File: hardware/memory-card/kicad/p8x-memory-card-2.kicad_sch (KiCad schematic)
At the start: 2 parts, among them U10 62256, U11 74HCT32

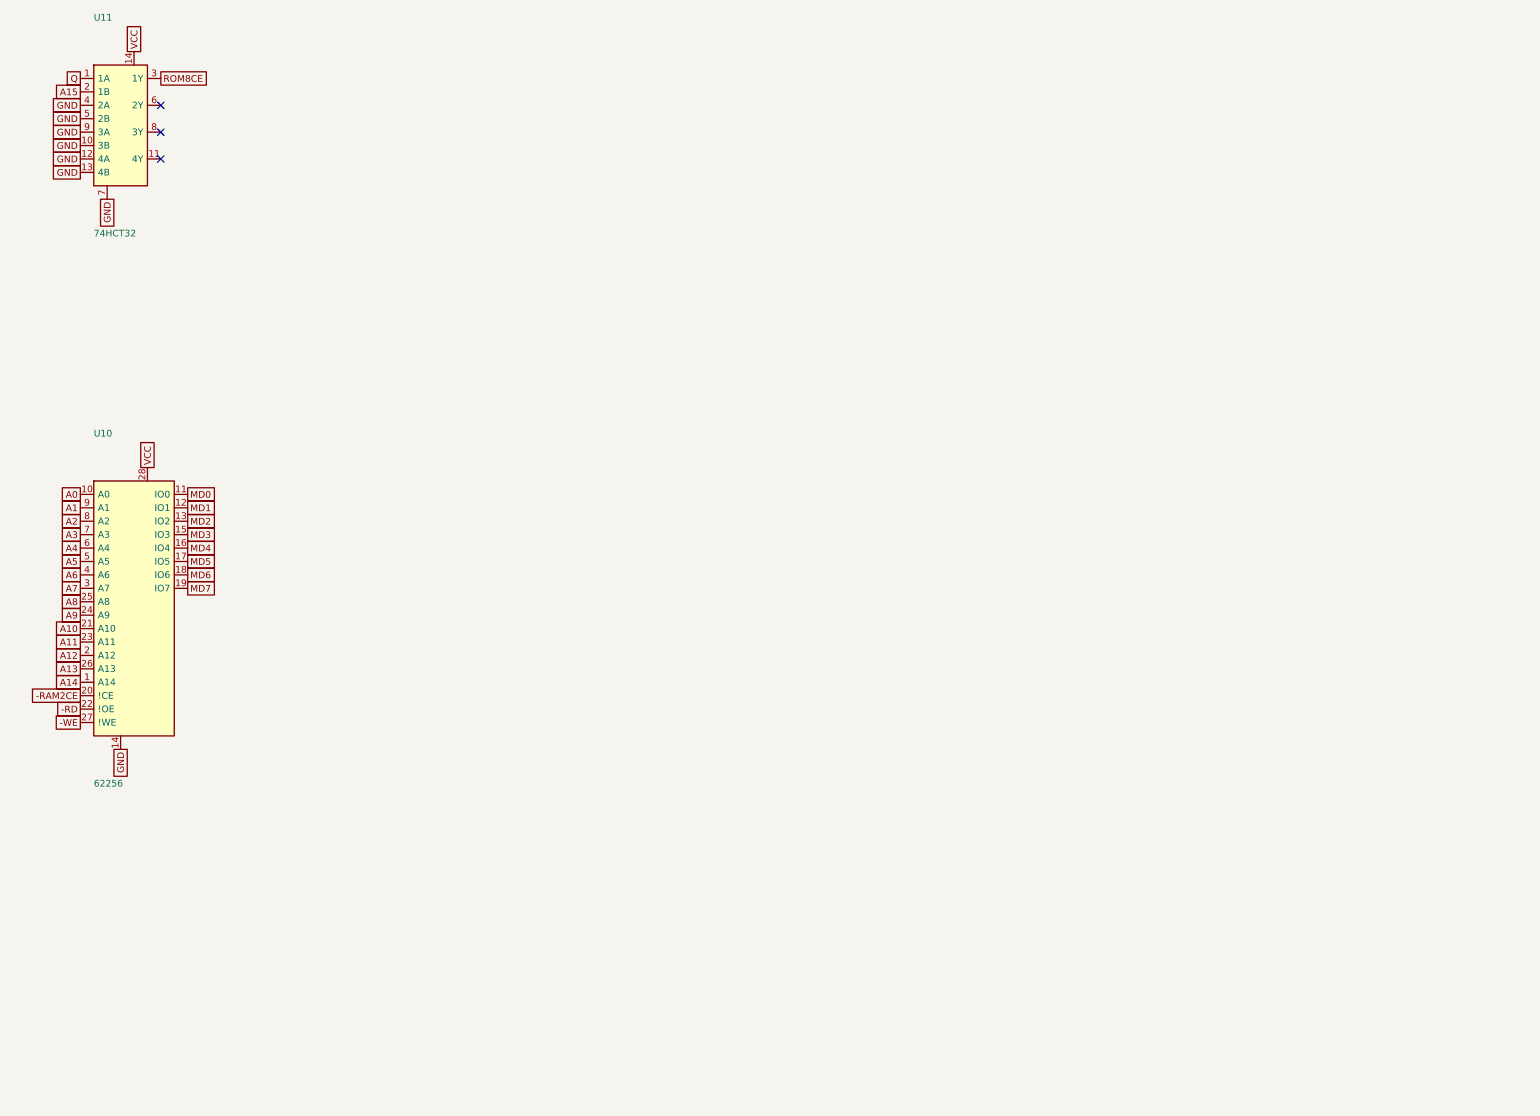
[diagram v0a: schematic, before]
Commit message: feat(sch): draw every P8X card schematic by function
Extend the functional-sheet grouping from the io-card to the control,
regbank, alu, memory, cf, ps2 and bustest cards. functional_sheets now
attaches unnamed glue gates, LEDs, resistors and connectors to the block
they share the most local nets with, so each block lists only its main
parts. A net with two or more pins on a sheet is now wired there even if
it continues elsewhere (its global name label rides on the wire), and
every wire is oriented by drawing side. The regbank gets one pointer per
sheet; the ps2 latches share a sheet with the AVR so the mailbox bus is
drawn. The bustest probe resistors use a straight-order RNISO8DSTR
drawing (the reversed B side forced every wire to cross and the sheet
fell back to labels). build_sch.sh now shows ELK fallbacks and clears old
numbered sheets before a build. All eight netlists match the boards,
ERC 0 errors; the boards change only in footprint link paths.

Co-Authored-By: Claude Opus 5.5 <noreply@anthropic.com>
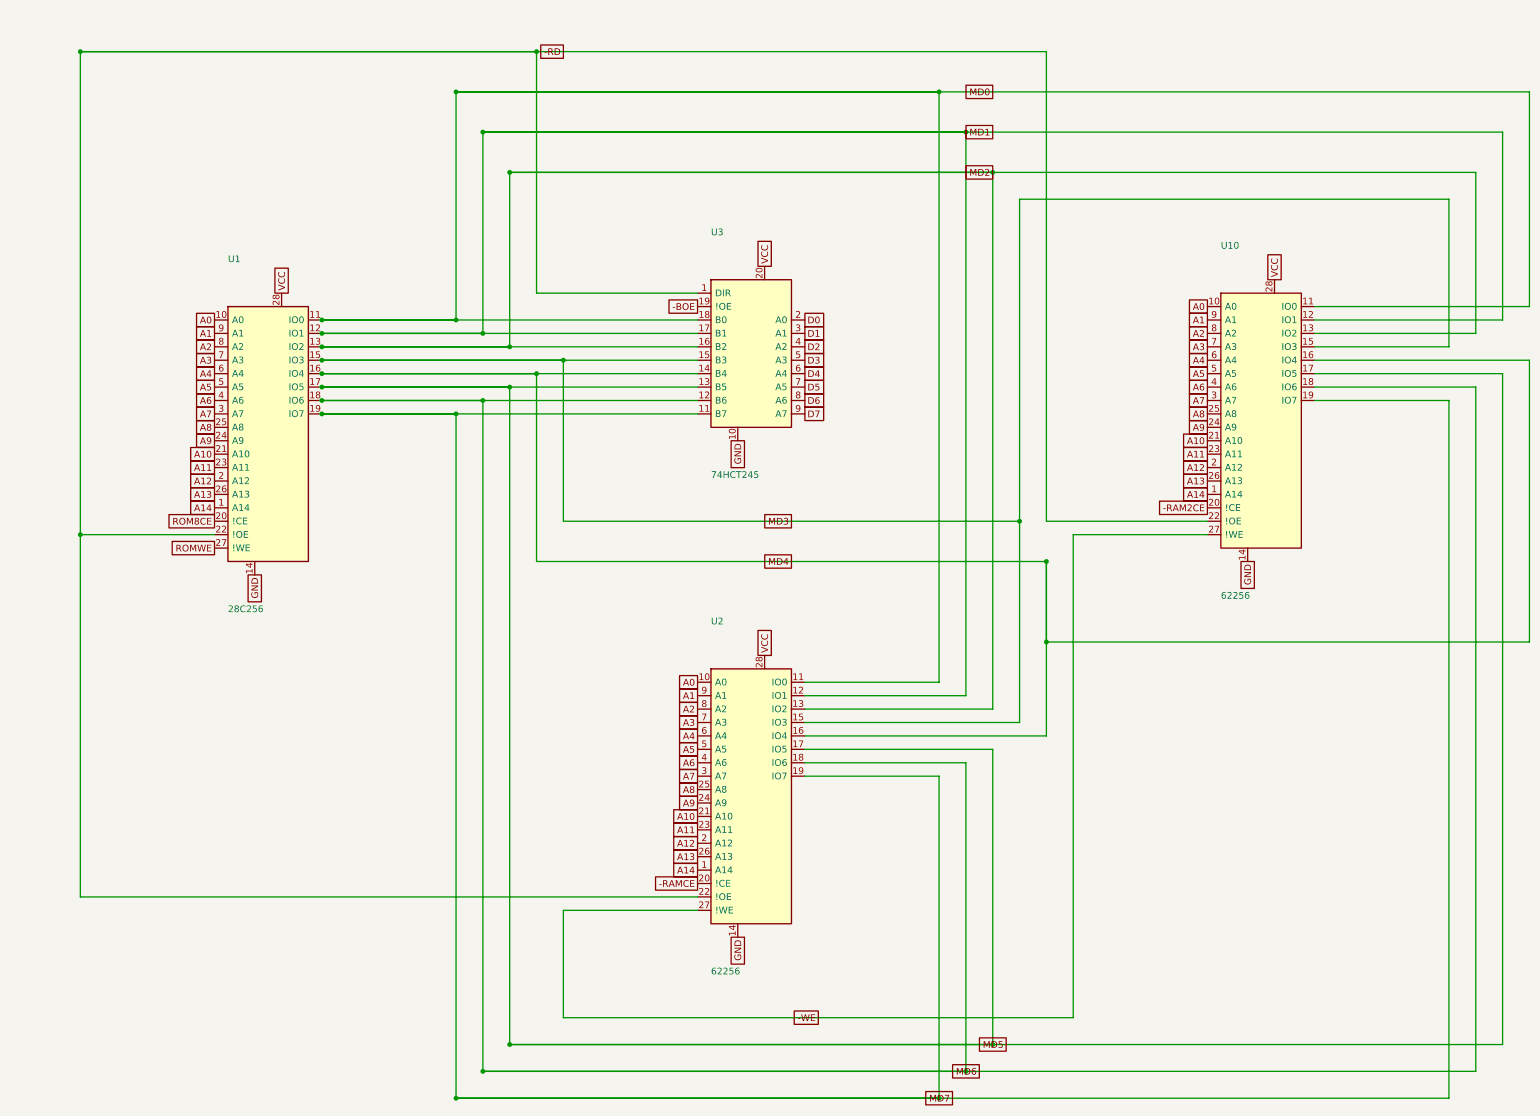
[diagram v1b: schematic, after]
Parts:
- removed U11: 74HCT32, Package_DIP:DIP-14_W7.62mm, symbol p8x:GATES14
- added U1: 28C256, Package_DIP:DIP-28_W15.24mm, symbol p8x:MEM28K8
- added U2: 62256, Package_DIP:DIP-28_W15.24mm, symbol p8x:MEM28K8
- added U3: 74HCT245, Package_DIP:DIP-20_W7.62mm, symbol p8x:74245
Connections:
- net -RD: now also U1.22 (!OE), U2.22 (!OE), U3.1 (DIR)
- net -WE: now also U2.27 (!WE)
- net A0: now also U1.10 (A0), U2.10 (A0)
- net A1: now also U1.9 (A1), U2.9 (A1)
- net A10: now also U1.21 (A10), U2.21 (A10)
- net A11: now also U1.23 (A11), U2.23 (A11)
- net A12: now also U1.2 (A12), U2.2 (A12)
- net A13: now also U1.26 (A13), U2.26 (A13)
- net A14: now also U1.1 (A14), U2.1 (A14)
- net A2: now also U1.8 (A2), U2.8 (A2)
- net A3: now also U1.7 (A3), U2.7 (A3)
- net A4: now also U1.6 (A4), U2.6 (A4)
- net A5: now also U1.5 (A5), U2.5 (A5)
- net A6: now also U1.4 (A6), U2.4 (A6)
- net A7: now also U1.3 (A7), U2.3 (A7)
- net A8: now also U1.25 (A8), U2.25 (A8)
- net A9: now also U1.24 (A9), U2.24 (A9)
- net GND: now also U1.14, U2.14, U3.10
- net MD0: now also U1.11 (IO0), U2.11 (IO0), U3.18 (B0)
- net MD1: now also U1.12 (IO1), U2.12 (IO1), U3.17 (B1)
- net MD2: now also U1.13 (IO2), U2.13 (IO2), U3.16 (B2)
- net MD3: now also U1.15 (IO3), U2.15 (IO3), U3.15 (B3)
- net MD4: now also U1.16 (IO4), U2.16 (IO4), U3.14 (B4)
- net MD5: now also U1.17 (IO5), U2.17 (IO5), U3.13 (B5)
- net MD6: now also U1.18 (IO6), U2.18 (IO6), U3.12 (B6)
- net MD7: now also U1.19 (IO7), U2.19 (IO7), U3.11 (B7)
- net ROM8CE: now also U1.20 (!CE)
- net VCC: now also U1.28, U2.28, U3.20
- new net -BOE: U3.19 (!OE)
- new net -RAMCE: U2.20 (!CE)
- new net D0: U3.2 (A0)
- new net D1: U3.3 (A1)
- new net D2: U3.4 (A2)
- new net D3: U3.5 (A3)
- new net D4: U3.6 (A4)
- new net D5: U3.7 (A5)
- new net D6: U3.8 (A6)
- new net D7: U3.9 (A7)
- new net ROMWE: U1.27 (!WE)
- no-connect marks 3 -> 0
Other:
- moved on the sheet: U10

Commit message: fix(memory): schematic and title are rev F
The KiCad schematic was drawn from gen_eagle's rev-E netlist (8 KB ROM
decode) and titled REV E, while the board is rev F (6 KB decode). The
rev-F transform moves out of gen_mem.py into mem_revf.py, which the board
and the schematic loader (p8x_card.py) both use. Schematic: "P8X MEMORY
CARD REV F (6K ROM DECODE)", ERC 0, netlist = ours. gen_eagle stays rev E
(Eagle flow frozen). Board pads and tracks unchanged; check_card PASS.

Also the backplane silk title is REV C, matching its schematic (was REV A).

Co-Authored-By: Claude Opus 5.5 <noreply@anthropic.com>
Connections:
- net ROM8CE renamed ROMCE
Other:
- title: P8X MEMORY CARD REV E -> P8X MEMORY CARD REV F (6K ROM DECODE)
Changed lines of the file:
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@@
 (kicad_sch (version 20231120) (generator "p8x_kicad_sch")
   (paper "A3")
-  (title_block (title "P8X MEMORY CARD REV E") (company "P8X") (comment 1 "ROM, RAM and data buffer") (comment 2 "Generated by generators/sch/p8x_kicad_sch.py from gen_eagle.py - do not edit"))
+  (title_block (title "P8X MEMORY CARD REV F (6K ROM DECODE)") (company "P8X") (comment 1 "ROM, RAM and data buffer") (comment 2 "Generated by generators/sch/p8x_kicad_sch.py from gen_eagle.py - do not edit"))
   (symbol (lib_id "p8x:74245") (at 187.96 109.22 0) (unit 1) (in_bom yes) (on_board yes) (dnp no)
     (property "Reference" "U3" (at 180.34 84.98 0) (effects (font (size 1.27 1.27)) (justify left)))
@@
   (global_label "A14" (shape passive) (at 86.36 137.16 180) (fields_autoplaced yes) (effects (font (size 1.27 1.27)) (justify right))
     (property "Intersheetrefs" "${INTERSHEET_REFS}" (at 86.36 137.16 0) (effects (font (size 1.27 1.27)) hide)))
-  (global_label "ROM8CE" (shape passive) (at 86.36 139.70 180) (fields_autoplaced yes) (effects (font (size 1.27 1.27)) (justify right))
+  (global_label "ROMCE" (shape passive) (at 86.36 139.70 180) (fields_autoplaced yes) (effects (font (size 1.27 1.27)) (justify right))
     (property "Intersheetrefs" "${INTERSHEET_REFS}" (at 86.36 139.70 0) (effects (font (size 1.27 1.27)) hide)))
   (global_label "ROMWE" (shape passive) (at 86.36 144.78 180) (fields_autoplaced yes) (effects (font (size 1.27 1.27)) (justify right))
